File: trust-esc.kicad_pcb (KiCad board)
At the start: 4 copper layers, 25 x 15.5 mm, 35 parts, among them J201 Conn_01x01_Male, J301 Conn_01x01_Male, J401 Conn_01x01_Male, Q201 BUK7M10-40EX, Q202 BUK7M10-40EX, Q301 BUK7M10-40EX, Q302 BUK7M10-40EX, Q401 BUK7M10-40EX, Q402 BUK7M10-40EX, U101 STSPIN32F0

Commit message: More additions and testing of PCB design
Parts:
- added C112: 6.8u, passive:C_0805, F.Cu at (90.6, 60.5)
- added J101: Conn_01x01_Male, connectors:pad_2.5x2.5mm, F.Cu at (98.5, 63.5)
- added J102: Conn_01x01_Male, connectors:pad_2.5x2.5mm, F.Cu at (98.5, 51.0)
- added eC111: 6.8u, passive:C_0805, F.Cu at (92.3, 60.5)
- C101, C102, C103, C105, C106, C107, C108, D101, L101, R201, R202, R301, R302, R401, R402, U101: moved to B.Cu
- moved R401 29.4 mm to (84.9, 59.9), turned to 0 degrees
- moved C108 28.5 mm to (84.9, 58.7), turned to 0 degrees
- moved R402 27.4 mm to (84.9, 57.8), turned to 0 degrees
- moved R301 26.6 mm to (84.9, 56.9), turned to 0 degrees
- moved C107 25.6 mm to (84.9, 55.7), turned to 0 degrees
- moved R302 24.8 mm to (84.9, 54.8), turned to 0 degrees
- moved R201 24.0 mm to (84.9, 53.8), turned to 0 degrees
- moved C401 23.4 mm to (94.0, 60.5), turned to 270 degrees
- moved C106 23.3 mm to (84.9, 52.7), turned to 0 degrees
- moved R202 22.7 mm to (84.9, 51.8), turned to 0 degrees
- moved C301 21.4 mm to (95.7, 60.5), turned to 270 degrees
- moved C102 21.3 mm to (95.1, 60.6), turned to 180 degrees
- moved U101 20.7 mm to (91.5, 55.5), turned to 180 degrees
- moved C101 20.1 mm to (96.6, 52.1), turned to 0 degrees
- moved D101 20.0 mm to (98.6, 54.4), turned to 90 degrees
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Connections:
- net /Half Bridge 1/VR renamed /VRU
- net /Half Bridge 2/VR renamed /VRV
- net /Half Bridge 3/VR renamed /VRW
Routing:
- net GND: track 0.00 -> 11.1 mm, vias 45 -> 8
- net /Half Bridge 1/GH: track 0.00 -> 8.17 mm, vias 0 -> 1
- net /Half Bridge 2/GH: track 0.00 -> 5.90 mm, vias 0 -> 1
- net /Half Bridge 3/GH: track 0.00 -> 5.25 mm, vias 0 -> 1
- net /OUTW: track 0.00 -> 4.31 mm, vias 0 -> 1
- net /OUTV: track 0.00 -> 4.11 mm, vias 0 -> 1
- net /OUTU: track 0.00 -> 3.97 mm, vias 0 -> 1
- net /Half Bridge 3/GL: track 0.00 -> 3.63 mm, vias 0 -> 1
- net /Half Bridge 2/GL: track 0.00 -> 2.70 mm, vias 0 -> 1
- net /Half Bridge 1/GL: track 0.00 -> 2.18 mm, vias 0 -> 1
- net +BATT: vias 48 -> 96
- added copper zone on B.Cu, net +BATT
- added copper zone on B.Cu, net GND
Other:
- outline, holes or cut-outs redrawn

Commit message: Testing some more PCB ideas
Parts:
- moved C106 0.70 mm to (84.2, 52.7)
- moved C107 0.70 mm to (84.2, 55.7)
- moved C108 0.70 mm to (84.2, 58.7)
- moved R201 0.70 mm to (84.2, 53.8)
- moved R202 0.70 mm to (84.2, 51.8)
- moved R301 0.70 mm to (84.2, 56.9)
- moved R302 0.70 mm to (84.2, 54.8)
- moved R401 0.70 mm to (84.2, 59.9)
- moved R402 0.70 mm to (84.2, 57.8)
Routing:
- net /Half Bridge 3/GH: track 5.25 -> 4.15 mm
- net /Half Bridge 2/GL: track 2.70 -> 3.66 mm
- net /OUTW: track 4.31 -> 5.20 mm
- net /OUTU: track 3.97 -> 3.17 mm
- net /Half Bridge 2/GH: track 5.90 -> 5.18 mm
- net /Half Bridge 1/GH: track 8.17 -> 8.84 mm
- net /Half Bridge 3/GL: track 3.63 -> 4.16 mm
- net /Half Bridge 1/GL: track 2.18 -> 2.69 mm
- net +BATT: vias 96 -> 108

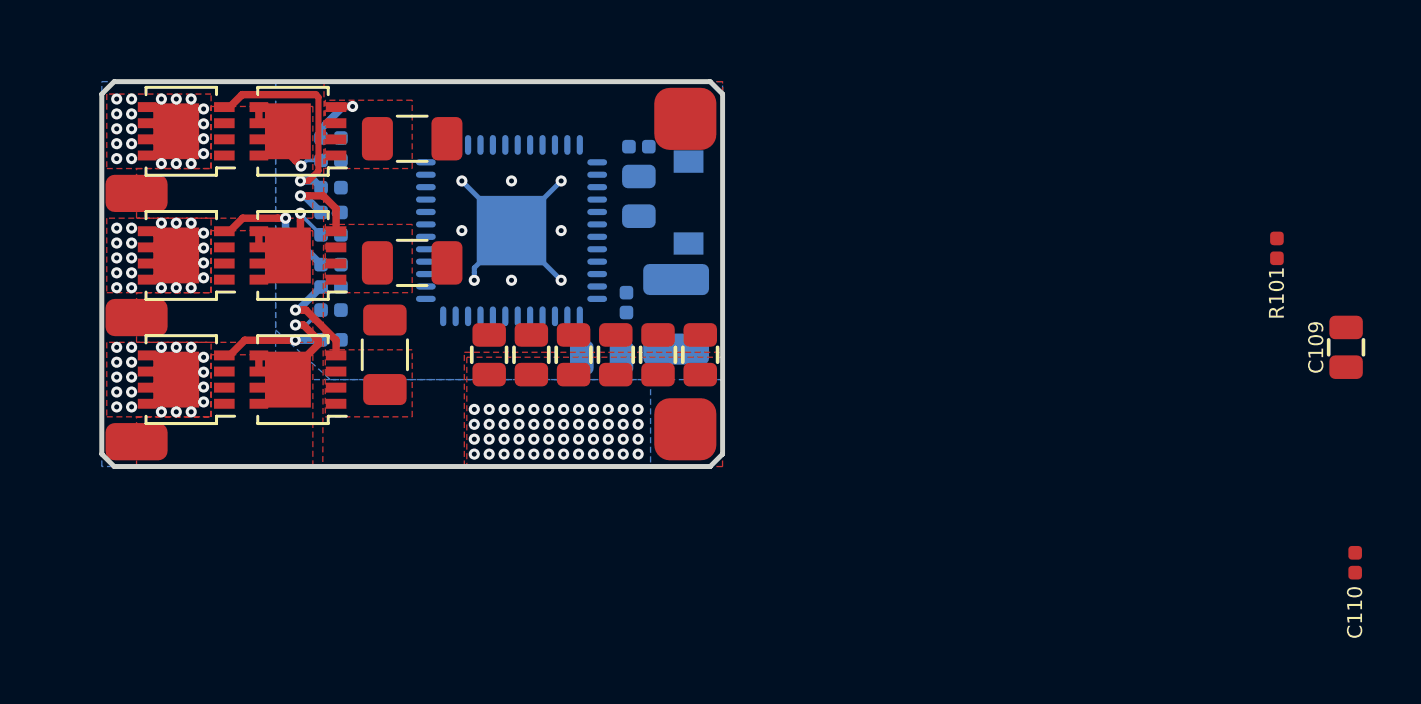
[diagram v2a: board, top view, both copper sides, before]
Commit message: New output pads
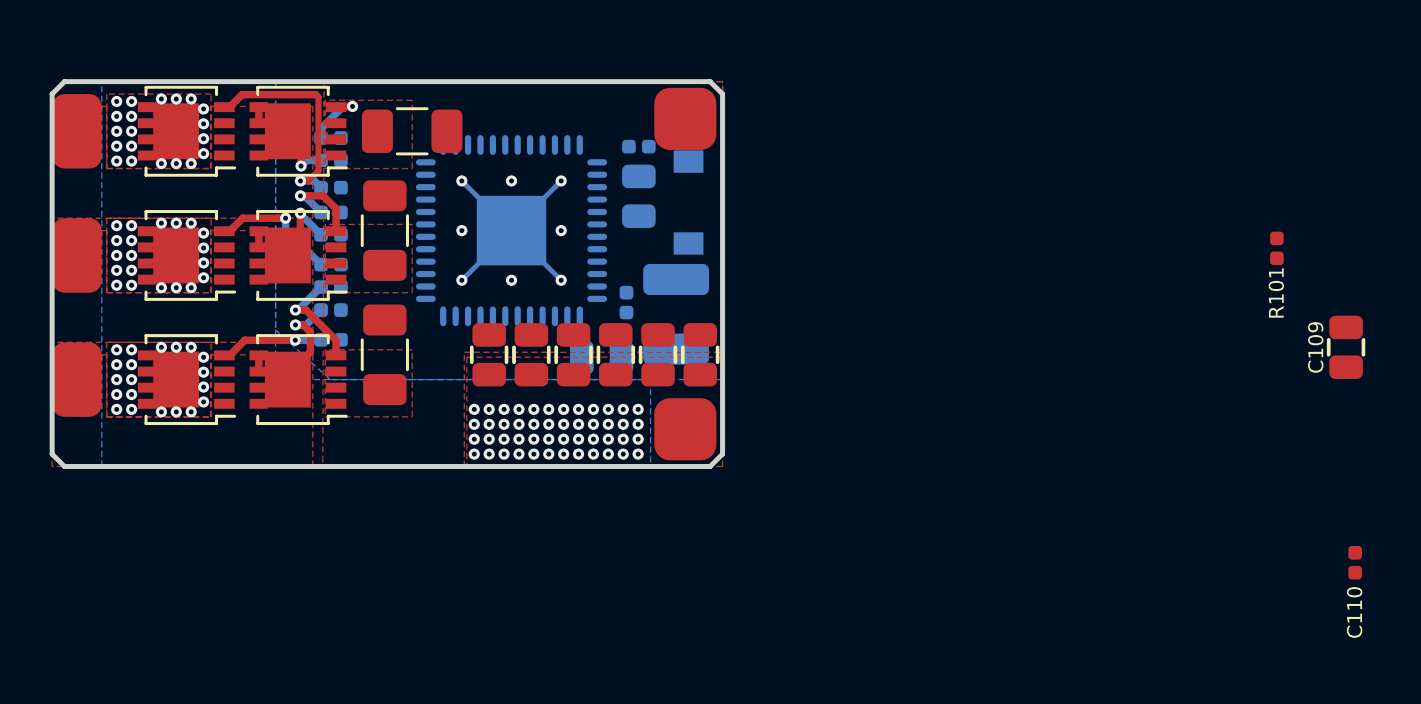
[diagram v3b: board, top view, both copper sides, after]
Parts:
- removed eC111: 6.8u, passive:C_0805
- added C111: 6.8u, passive:C_0805, F.Cu at (92.3, 60.5)
- J201, J301, J401: footprint connectors:pad_1.5x2.5mm -> connectors:pad_3.0x2.0mm
- moved J201 3.47 mm to (74.0, 51.5)
- moved J301 3.47 mm to (74.0, 56.5)
- moved J401 3.47 mm to (74.0, 61.5)
- moved R303 1.70 mm to (86.4, 55.5), turned to 90 degrees
- moved R203 0.30 mm to (87.5, 51.5)
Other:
- board size 25 x 15.5 mm -> 27 x 15.5 mm

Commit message: First routing complete
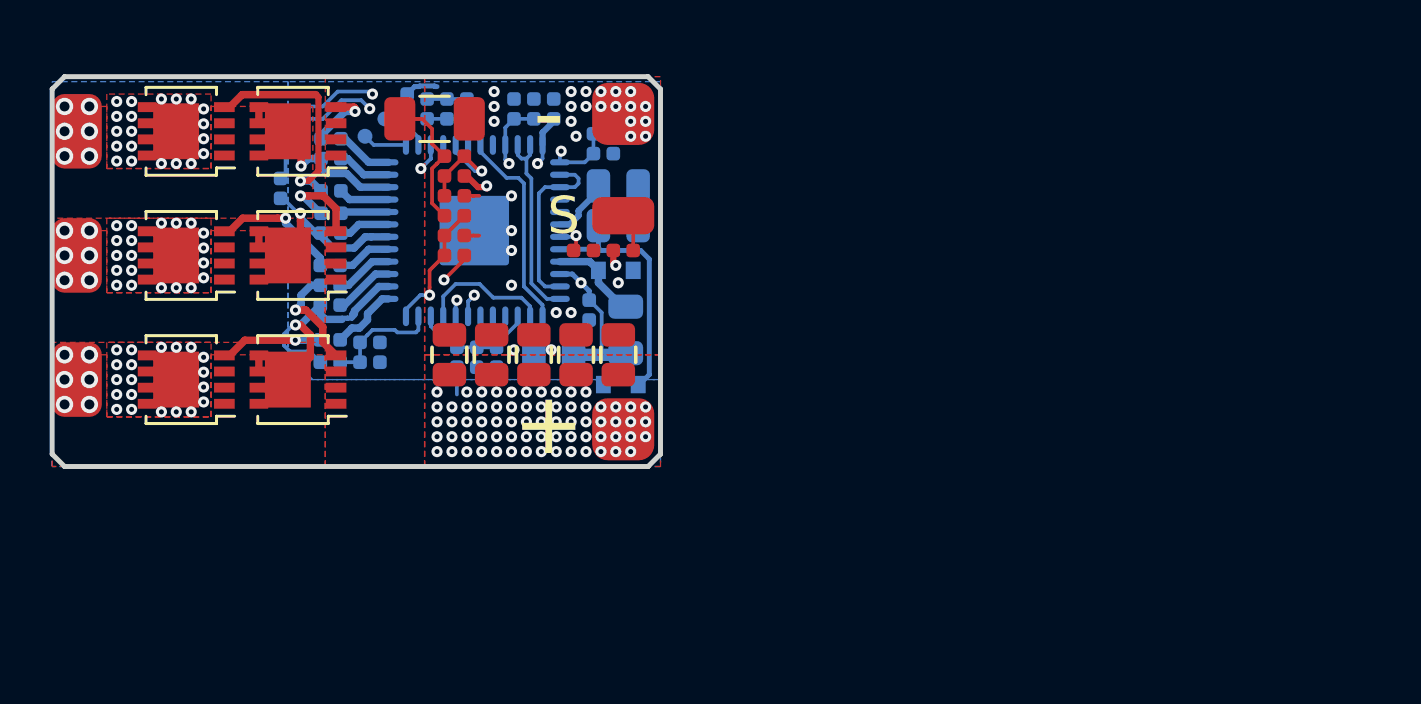
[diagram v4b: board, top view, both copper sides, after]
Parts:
- removed C109, C201, C301, C401: 6.8u, passive:C_0805
- removed C110: 0.1u, passive:C_0402_1005Metric_Rounded
- removed R101: 10k, passive:R_0402_1005Metric_Rounded
- removed R203, R303, R403: 1m, Resistor_SMD:R_1206_3216Metric
- added C113: 6.8u, passive:C_0805, F.Cu at (92.4, 60.5)
- added C114: 6.8u, passive:C_0805, F.Cu at (94.1, 60.5)
- added C116: 6.8u, passive:C_0805, F.Cu at (95.8, 60.5)
- added C117: 1n, passive:C_0402_1005Metric_Rounded, F.Cu at (89.2, 55.7)
- added C118: 100n, passive:C_0402_1005Metric_Rounded, B.Cu at (90.9, 60.6)
- added C119: 0.1u, passive:C_0402_1005Metric_Rounded, F.Cu at (94.4, 56.3)
- added C501: 22p, passive:C_0402_1005Metric_Rounded, B.Cu at (88.1, 50.6)
- added C701: 47p, passive:C_0402_1005Metric_Rounded, B.Cu at (95.2, 52.4)
- added C801: 47p, passive:C_0402_1005Metric_Rounded, B.Cu at (92.4, 50.6)
- added C802: 47p, passive:C_0402_1005Metric_Rounded, B.Cu at (85.8, 60.0)
- added D102: NSR05T30XV2T5G, Diode_SMD:D_SOD-523, B.Cu at (95.9, 61.7)
- added J103: Conn_01x01_Male, connectors:pad_1.5x2.5mm, F.Cu at (96.0, 54.9)
- added J104: Conn_01x01_Male, TestPoint:TestPoint_Pad_D1.0mm, B.Cu at (85.6, 51.7)
- added J105: Conn_01x01_Male, TestPoint:TestPoint_Pad_D1.0mm, B.Cu at (86.4, 51.0)
- added R102: 100, passive:R_0402_1005Metric_Rounded, F.Cu at (96.0, 56.3)
- added R103: 1m, Resistor_SMD:R_1206_3216Metric, F.Cu at (88.4, 51.0)
- added R108: 47k, passive:R_0402_1005Metric_Rounded, F.Cu at (89.2, 56.5)
- added R109: 2.94k, passive:R_0402_1005Metric_Rounded, F.Cu at (89.2, 54.9)
- added R110: 47k, passive:R_0402_1005Metric_Rounded, B.Cu at (89.3, 60.6)
- added R111: 10k, passive:R_0402_1005Metric_Rounded, B.Cu at (90.1, 60.6)
- added R501: 1k, passive:R_0402_1005Metric_Rounded, F.Cu at (89.2, 52.5)
- added R502: 1k, passive:R_0402_1005Metric_Rounded, B.Cu at (87.3, 50.4)
- added R503: 47k, passive:R_0402_1005Metric_Rounded, F.Cu at (89.2, 54.1)
- added R504: 47k, passive:R_0402_1005Metric_Rounded, F.Cu at (89.2, 53.3)
- added R505: 47k, passive:R_0402_1005Metric_Rounded, B.Cu at (89.7, 50.6)
- added R506: 47k, passive:R_0402_1005Metric_Rounded, B.Cu at (88.9, 50.6)
- added R701: 47k, passive:R_0402_1005Metric_Rounded, B.Cu at (82.2, 53.8)
- added R702: 10k, passive:R_0402_1005Metric_Rounded, B.Cu at (95.2, 51.6)
- added R801: 47k, passive:R_0402_1005Metric_Rounded, B.Cu at (83.0, 51.4)
- added R802: 10k, passive:R_0402_1005Metric_Rounded, B.Cu at (91.6, 50.6)
- added R803: 47k, passive:R_0402_1005Metric_Rounded, B.Cu at (84.2, 60.8)
- added R804: 10k, passive:R_0402_1005Metric_Rounded, B.Cu at (85.8, 60.8)
- C104: moved to B.Cu
- D101: value PMEG4010 -> NSR05T30XV2T5G; footprint Diode_SMD:D_SOD-123 -> Diode_SMD:D_SOD-523
- L101: footprint Inductor_SMD:L_1210_3225Metric -> Inductor_SMD:L_0805_2012Metric
- moved C104 5.44 mm to (95.8, 55.3), turned to 180 degrees
- moved D101 4.00 mm to (95.7, 57.1), turned to 0 degrees
- moved C101 3.75 mm to (93.2, 50.6), turned to 90 degrees
- moved J102 2.51 mm to (96.0, 50.8)
- moved J101 2.50 mm to (96.0, 63.5)
- moved L101 2.13 mm to (96.1, 59.5)
- moved C102 1.93 mm to (93.2, 60.6)
- moved C111 1.60 mm to (90.7, 60.5)
- moved C112 1.60 mm to (89.0, 60.5)
- moved C103 1.53 mm to (94.6, 58.7)
- moved U101 1.50 mm to (90.0, 55.5)
- moved C105 0.93 mm to (95.8, 53.7), turned to 180 degrees
- moved C108 0.20 mm to (84.2, 58.5)
- moved R201 0.13 mm to (84.2, 53.9)
- moved R402 0.08 mm to (84.2, 57.7)
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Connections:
- net /OUTU renamed /PHASEU
- net /OUTV renamed /PHASEV
- net /OUTW renamed /PHASEW
- C104 pad 2: +BATT -> /VBAT_IN
- Q202 pad 1: /VRU -> /VR
- Q202 pad 2: /VRU -> /VR
- Q202 pad 3: /VRU -> /VR
- Q302 pad 1: /VRV -> /VR
- Q302 pad 2: /VRV -> /VR
- Q302 pad 3: /VRV -> /VR
- Q402 pad 1: /VRW -> /VR
- Q402 pad 2: /VRW -> /VR
- Q402 pad 3: /VRW -> /VR
- U101 pad 1: Net-(U101-Pad1) -> /OP4P
- U101 pad 11: Net-(U101-Pad11) -> /OP4O
- U101 pad 12: Net-(U101-Pad12) -> /OP3O
- U101 pad 13: Net-(U101-Pad13) -> /OP2O
- U101 pad 14: Net-(U101-Pad14) -> /OP1O
- U101 pad 15: Net-(U101-Pad15) -> /VBAT_SENSE
- U101 pad 19: Net-(U101-Pad19) -> Net-(R102-Pad1)
- U101 pad 2: Net-(U101-Pad2) -> /OP4O
- U101 pad 21: Net-(U101-Pad21) -> /OP1O
- U101 pad 22: Net-(U101-Pad22) -> /OP1O
- U101 pad 23: Net-(U101-Pad23) -> /OP1P
- U101 pad 24: Net-(U101-Pad24) -> /OC
- U101 pad 3: Net-(U101-Pad3) -> /OP4O
- U101 pad 37: Net-(U101-Pad37) -> /SWIO
- U101 pad 38: Net-(U101-Pad38) -> /SWCLK
- U101 pad 39: Net-(U101-Pad39) -> Net-(R102-Pad1)
- U101 pad 41: Net-(U101-Pad41) -> /OP2P
- U101 pad 42: Net-(U101-Pad42) -> /OP2N
- U101 pad 43: Net-(U101-Pad43) -> /OP2O
- U101 pad 45: Net-(U101-Pad45) -> /OP3P
- U101 pad 46: Net-(U101-Pad46) -> /OP3O
- U101 pad 47: Net-(U101-Pad47) -> /OP3O
- U101 pad 7: Net-(U101-Pad7) -> /NRST
- U101 pad 8: +BATT -> /VBAT_IN
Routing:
- net +3V3: track 0.00 -> 31.0 mm, vias 0 -> 4
- net /OP4P: track 0.00 -> 17.9 mm, vias 0 -> 2
- net Net-(R102-Pad1): track 0.00 -> 15.6 mm, vias 0 -> 3
- net /OP3P: track 0.00 -> 12.7 mm, vias 0 -> 2
- net /OP2O: track 0.00 -> 12.1 mm
- net /VBAT_IN: track 0.00 -> 10.0 mm
- net GND: track 11.3 -> 3.22 mm, vias 8 -> 30
- net /OP3O: track 0.00 -> 7.94 mm
- net /OP4O: track 0.00 -> 7.23 mm
- net /PHASEW: track 4.94 -> 11.7 mm, vias 1 -> 7
- net /OP1O: track 0.00 -> 6.70 mm
- net /VR: track 0.00 -> 5.68 mm
- net /OC: track 0.00 -> 5.24 mm, vias 0 -> 1
- net /OP1P: track 0.00 -> 4.79 mm
- net /PHASEU: track 3.17 -> 7.73 mm, vias 1 -> 7
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- added copper zone on In1.Cu, net +BATT
- added copper zone on In2.Cu, net +BATT
- added copper zone on F.Cu, net /VR
- added copper zone on In1.Cu, net GND
- added copper zone on In2.Cu, net GND
- removed copper zone on F.Cu, net /VRU
- removed copper zone on F.Cu, net /VRV
- removed copper zone on F.Cu, net /VRW
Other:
- board size 27 x 15.5 mm -> 24.5 x 15.7 mm
- board text added: "+"
- board text added: "-"
- board text added: "S"

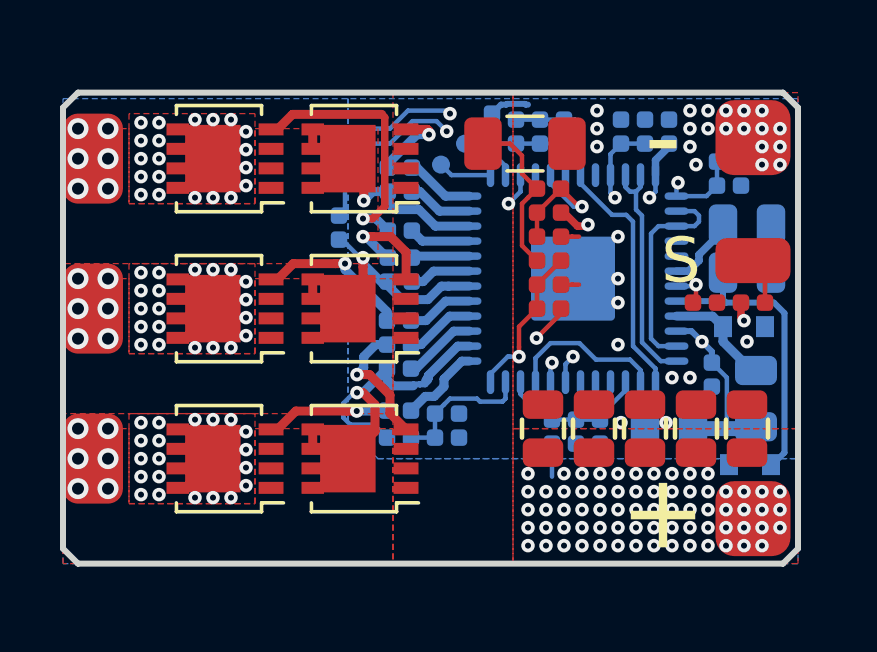
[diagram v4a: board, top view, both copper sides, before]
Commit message: New current sense resistor + silk fixes
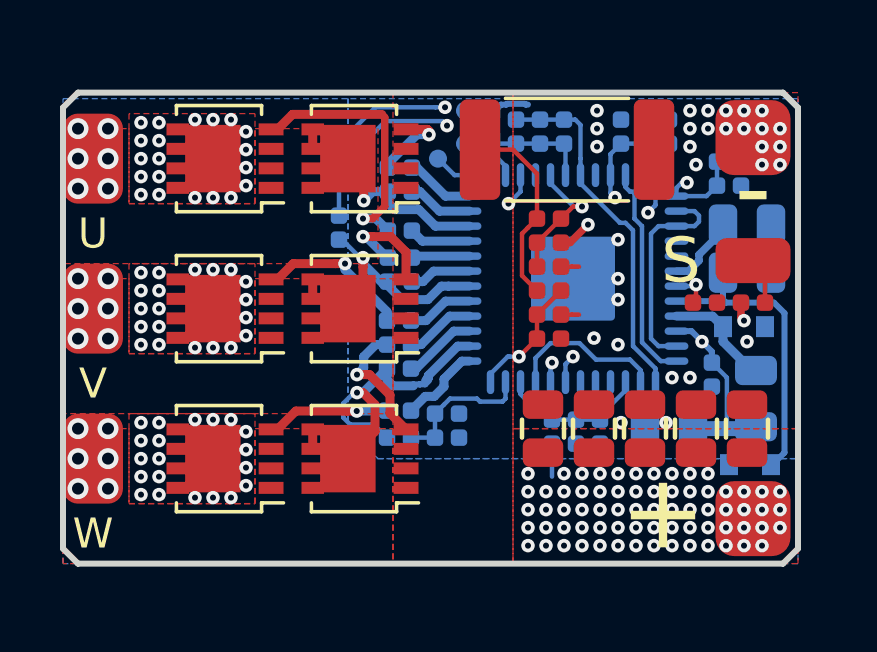
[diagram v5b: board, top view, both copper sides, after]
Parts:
- added J106: Conn_01x01_Male, connectors:pad_circ_0.6mm, B.Cu at (86.4, 49.9)
- J104, J105: footprint TestPoint:TestPoint_Pad_D1.0mm -> connectors:pad_circ_0.6mm
- R103: footprint Resistor_SMD:R_1206_3216Metric -> Resistor_SMD:R_2512_6332Metric
- moved R103 1.41 mm to (89.8, 51.2)
- moved C117 1.00 mm to (89.2, 56.7)
- moved R108 1.00 mm to (89.2, 57.5)
- moved R109 1.00 mm to (89.2, 55.9)
- moved R501 1.00 mm to (89.2, 53.5)
- moved R503 1.00 mm to (89.2, 55.1)
- moved R504 1.00 mm to (89.2, 54.3)
- moved J104 0.22 mm to (85.5, 51.5)
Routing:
- net +3V3: track 31.0 -> 27.1 mm
- net /OC: track 5.24 -> 4.24 mm
- net /VR: track 5.68 -> 6.64 mm
- net GND: track 3.22 -> 4.16 mm
- net /OP4P: track 17.9 -> 18.5 mm
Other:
- board text added: "CLK"
- board text added: "GND"
- board text added: "IO"
- board text added: "U"
- board text added: "V"
- board text added: "W"
